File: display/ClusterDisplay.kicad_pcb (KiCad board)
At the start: 4 copper layers, 174.9 x 101.8 mm, 164 parts, among them J1 Verdin iMX95 Hexa 8GB WB IT, J10 RTC coin cell, J11 Molex KK-254 22-27-2041, rota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, J12 Samtec TSW-103-07-G-S A55 con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, J13 Samtec TSW-105-07-G-S USB_1 O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, J14 JST XH B5B-XH-A balanced line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, J15 JST XH B3B-XH-A electret micr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, J16 MFi coprocessor access I2C_1 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, J17 GCT USB4105-GF-A USB-C 2.0 ho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, J2 Phoenix MKDS 1,5/3-5,08 power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, J3 Molex KK-254 22-27-2031 priva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, J4 TST040HDBC-42 panel, J8 Samtec TSW-108-07-G-S JTAG (b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, J9 Samtec TSW-104-07-G-S buttons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, Q1 PMV55ENEA (AEC-Q101, 60V/20V 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, Q2 PMV55ENEA (AEC-Q101, 60V/20V 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, Q3 PMV55ENEA ignition wake pulld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, U1 LM74930-Q1, U10 TLV767-Q1 (3.3 V audio AVDD), U11 TPS2557-Q1, U12 TPD4E05U06-Q1 line-out ESD, U13 TPD4E05U06-Q1 mic ESD, U14 TPD4E05U06-Q1 USB ESD, U2 LM61460-Q1, U3 TLV767-Q1, U4 TCAN1044V-Q1, U6 TPS65131-Q1, U7 TPS61165-Q1, U8 TPS22918-Q1 (AEC-Q100 G2) dia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, U9 TAC5112-Q1

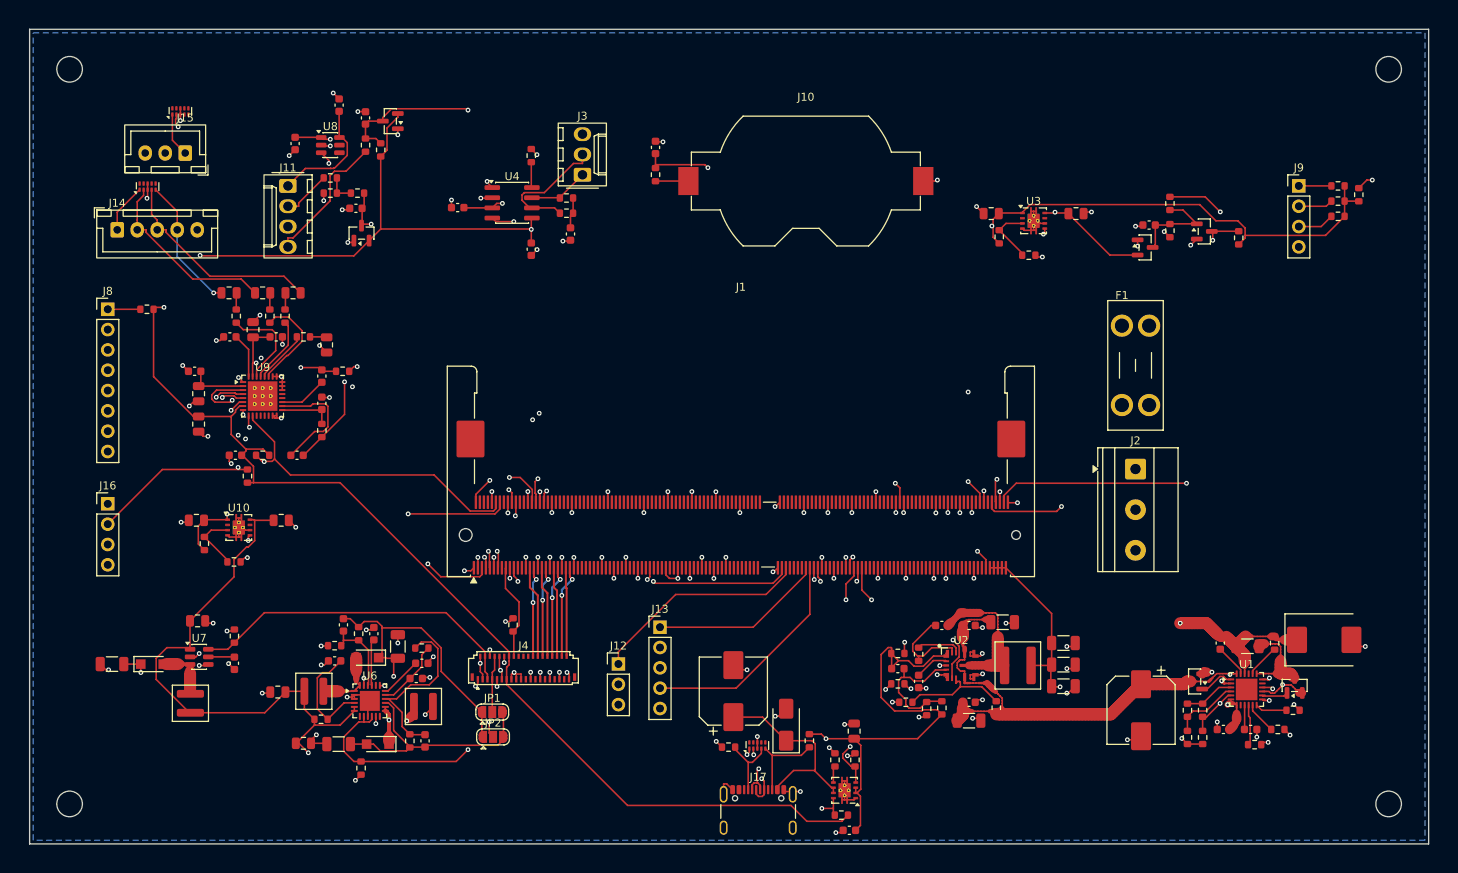
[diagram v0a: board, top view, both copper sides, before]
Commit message: Fix what would stop the boards becoming a product: Verdin mounting, FETs, CarPlay header
Product review 2026-10-18 (docs/electrical-review.md section 8a):
- display: Toradex's four M2 standoffs (S1/S2 2.5 mm module hold-down for
  vibration, S3/S4 7.0 mm for the Verdin Industrial Heatsink) at the design
  guide's Fig 113 positions, GND rings kept on the outer layers; the module
  keepout now follows the real module outline (the module is not centred
  on the socket; the strip under its far edge was open). 178.2 x 105.0 mm.
- display: J16 is a 1x6 MFi daughterboard header with a 5 V supply switched
  by U15 (TPS22918-Q1) from Verdin GPIO_3, as LIVI's carPlayMfiPowerGpio
  expects; the Apple part itself stays on the daughterboard (NDA).
- both: the LM74930 FET pair is Vishay SQJ460AEP (PowerPAK SO-8L, 8.7 mohm,
  IDM 180 A) instead of the NRND SOT-23 PMV55ENEA (X-01, X-02, D-05).
- gauges: 2.2 uH XAL5030-222MEC and 16 V 1210 output caps per the LMR33630
  datasheet (G-14), 1 uF CVS (G-17); inner small gauges at the measured
  +/-118 mm (owner photos), arrows midway between each side's gauges.
- display: 16 V 1210 panel-bias output caps (D-03); bidirectional
  TPD4E02B04-Q1 on the line-out legs (D-11).
- docs: depth stack-up first pass, Toradex supply/thermal/BSP questions,
  an RFQ for wider-temperature small displays, BOM supply-risk note.
Both boards: 0 unconnected, DRC only in the accepted categories, BOM
coverage and fab gate pass; review_netlist gauges 62/62, display only the
pre-existing U6 decoupling distance.

Co-Authored-By: Claude Opus 5.5 <noreply@anthropic.com>
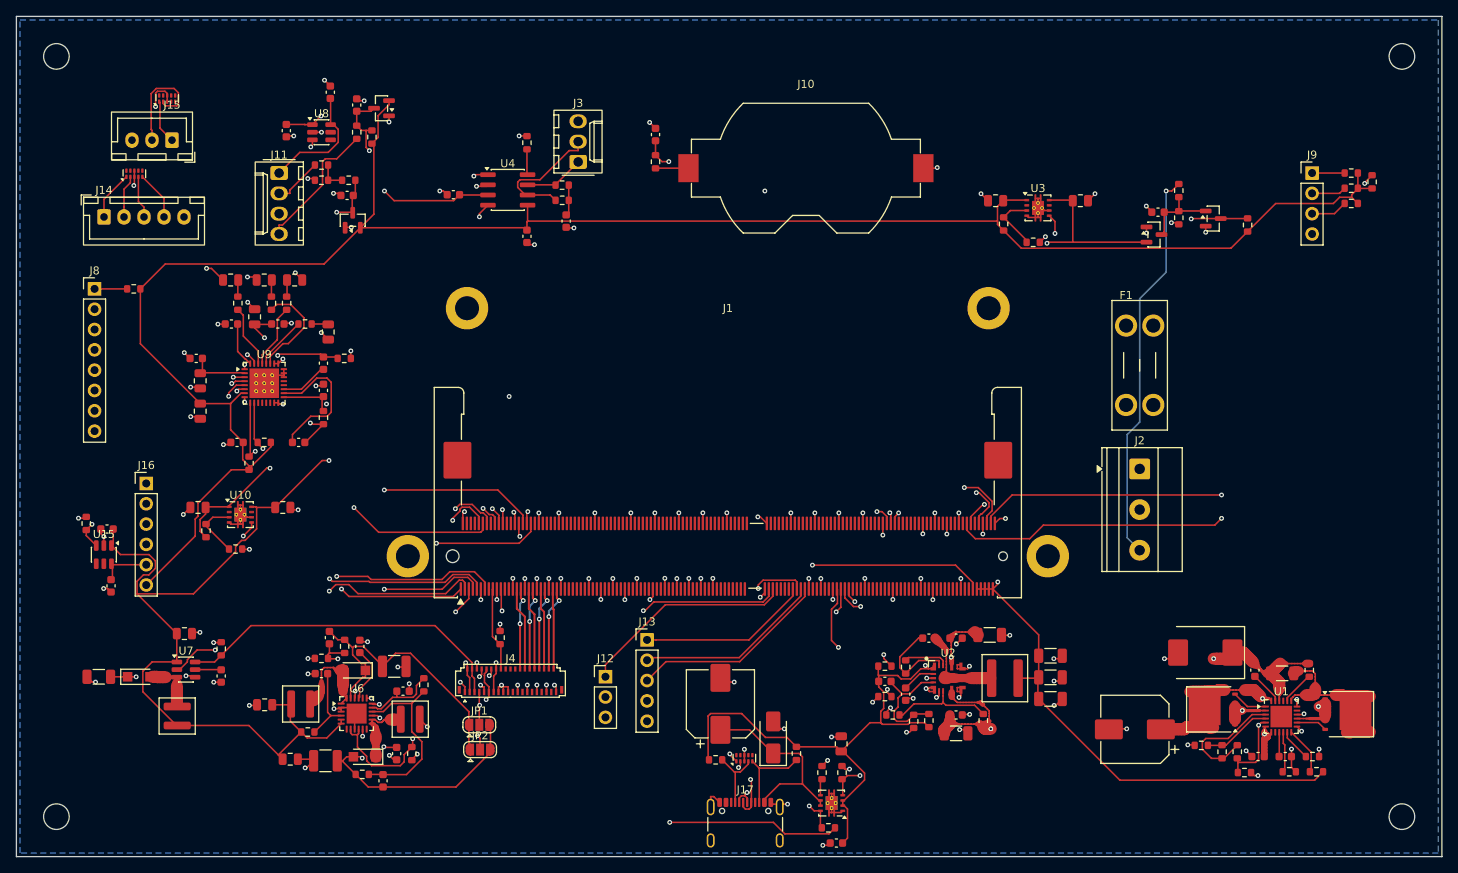
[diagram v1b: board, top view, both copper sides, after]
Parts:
- added C83: 1u MFi switch CIN, Capacitor_SMD:C_0603_1608Metric, F.Cu at (132.2, 160.1)
- added C84: 1u MFi 5V out, Capacitor_SMD:C_0603_1608Metric, F.Cu at (132.7, 167.2)
- added R74: 100k MFi switch off in reset, Resistor_SMD:R_0603_1608Metric, F.Cu at (129.6, 159.4)
- added S1: M2x0.4 SMD standoff 2.5 mm, MountingHole:MountingHole_2.2mm_M2_Pad, F.Cu at (177.2, 132.5)
- added S2: M2x0.4 SMD standoff 2.5 mm, MountingHole:MountingHole_2.2mm_M2_Pad, F.Cu at (242.4, 132.5)
- added S3: M2x0.4 SMD standoff 7.0 mm, MountingHole:MountingHole_2.2mm_M2_Pad, F.Cu at (169.8, 163.5)
- added S4: M2x0.4 SMD standoff 7.0 mm, MountingHole:MountingHole_2.2mm_M2_Pad, F.Cu at (249.8, 163.5)
- added U15: TPS22918-Q1 (AEC-Q100 G2) MFi 5V switch, Package_TO_SOT_SMD:SOT-23-6, F.Cu at (131.8, 163.3)
- C46, C47: footprint Capacitor_SMD:C_1206_3216Metric -> Capacitor_SMD:C_1210_3225Metric
- J16: value MFi coprocessor access I2C_1 + reset (TBD, DNP) -> MFi daughterboard header I2C_1, reset, switched 5V, 1V8 (DNP); footprint Connector_PinHeader_2.54mm:PinHeader_1x04_P2.54mm_Vertical -> Connector_PinHeader_2.54mm:PinHeader_1x06_P2.54mm_Vertical
- Q1: value PMV55ENEA (AEC-Q101, 60V/20V VGS) diode -> SQJ460AEP (AEC-Q101, 60V/20V VGS) diode; footprint Package_TO_SOT_SMD:SOT-23 -> Package_SO:PowerPAK_SO-8L_Single
- Q2: value PMV55ENEA (AEC-Q101, 60V/20V VGS) pass -> SQJ460AEP (AEC-Q101, 60V/20V VGS) pass; footprint Package_TO_SOT_SMD:SOT-23 -> Package_SO:PowerPAK_SO-8L_Single
- U12: value TPD4E05U06-Q1 line-out ESD -> TPD4E02B04-Q1 line-out ESD (bidirectional, review D-11)
- moved D1 15.0 mm to (269.5, 175.5), turned to 180 degrees
- moved C45 11.7 mm to (168.4, 188.1), turned to -90 degrees
- moved R15 8.23 mm to (283.4, 190.4)
- moved Q2 7.45 mm to (287.2, 183.2), turned to 0 degrees
- moved R40 7.28 mm to (164.1, 190.7), turned to 0 degrees
- moved C49 7.24 mm to (166.7, 191.5)
- moved R6 6.83 mm to (274.4, 190.5), turned to 0 degrees
- moved R5 6.76 mm to (273.5, 187.9)
- moved R7 6.76 mm to (271.6, 187.9), turned to 90 degrees
- moved R43 6.60 mm to (170.3, 188.1)
- moved C3 5.50 mm to (275.7, 177.7)
- moved R3 5.50 mm to (282.9, 188.5)
- moved R4 5.50 mm to (280.0, 190.4)
- moved C2 5.50 mm to (276.1, 188.5)
- moved C4 5.50 mm to (279.5, 188.5)
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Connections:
- J1 pad 210: (no net) -> MFI_PWR_EN
- Q1 pad 1: DGATE -> COMMON
- Q1 pad 3: +12V_PROT -> COMMON
- Q2 pad 1: HGATE -> COMMON
- Q2 pad 3: SENSE_OUT -> COMMON
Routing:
- net MFI_PWR_EN: track 0.00 -> 107.3 mm, vias 0 -> 2
- net +1V8: track 318.5 -> 353.5 mm, vias 4 -> 2
- net JTAG_TMS: track 99.1 -> 66.4 mm
- net +12V_PROT: track 65.7 -> 97.9 mm, vias 2 -> 4
- net I2C1_SCL: track 78.9 -> 58.7 mm, vias 3 -> 2
- net RECOVERY: track 69.7 -> 85.3 mm, vias 2 -> 1
- net DIAL_CLICK: track 93.2 -> 108.7 mm, vias 2 -> 3
- net GND: track 207.6 -> 220.8 mm, vias 145 -> 149
- net SENSE_OUT: track 11.3 -> 23.3 mm
- net PANEL_BIAS_EN: track 49.5 -> 37.8 mm
- net MIC_N: track 44.7 -> 55.4 mm, vias 2 -> 1
- net VBACKUP: track 72.9 -> 83.4 mm
- net MFI_RST_N: track 104.6 -> 95.0 mm
- net SW_SENSE: track 6.28 -> 15.8 mm
- net I2S_FSYNC: track 55.2 -> 46.0 mm, vias 3 -> 2
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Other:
- board size 174.9 x 101.8 mm -> 178.2 x 105 mm

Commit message: Six layers with solid GND planes, a field-solved DSI geometry, and the RGB variant routed
Both boards and display-rgb/ move to JLC06161H-3313 six-layer: F / In1 GND /
In2 / In3 with the +5V or +3V3 pour / In4 GND / B. Every net class except GND
is restricted to F, In2, In3 and B in the router input (FreeRouting 2.2.4
ignores a layer_rule "active off"), and review/layout_checks.py now fails a
board with any track on In1 or In4. All three boards: 0 unconnected under
kicad-cli DRC, accepted categories only, no copper but GND fill on the planes.

- DSI pairs are 0.16 mm, field-solved on the new stack-up at 96.4-103.1 ohm
  differential (review/dsi_impedance.py); board minimum track 0.15 mm.
- gauges/ routes VIN_PROT, VIN_FUSED and +5V at 0.4 mm from the start; every
  power net now passes the 20 K current check, and nothing crosses the buck's
  switch node (P-07).
- Panel bias +5.98 V / -6.05 V, inside the ICNL9707's rating; fab/README.md
  gives a diode-test check of the panel's pin polarity before JP1/JP2.
- display-rgb/ brought up to date with display/ (standoffs, FETs, audio,
  USB-C, MFi header), RGB parts renumbered, routed; still not a fab candidate
  while its panel connector is a placeholder.
- FreeRouting runs end at routing: (postroute off) in the DSN, a job timeout
  as backstop; one in-place attempt, since retries of one DSN are identical.
- The OV/UV divider tops are pulled to the LM74930 SW pin.
- docs/electrical-review.md section 8b records the measured results; the
  display/ battery path on inner copper (D-02 residual) is still open.

Co-Authored-By: Claude Opus 5.5 <noreply@anthropic.com>
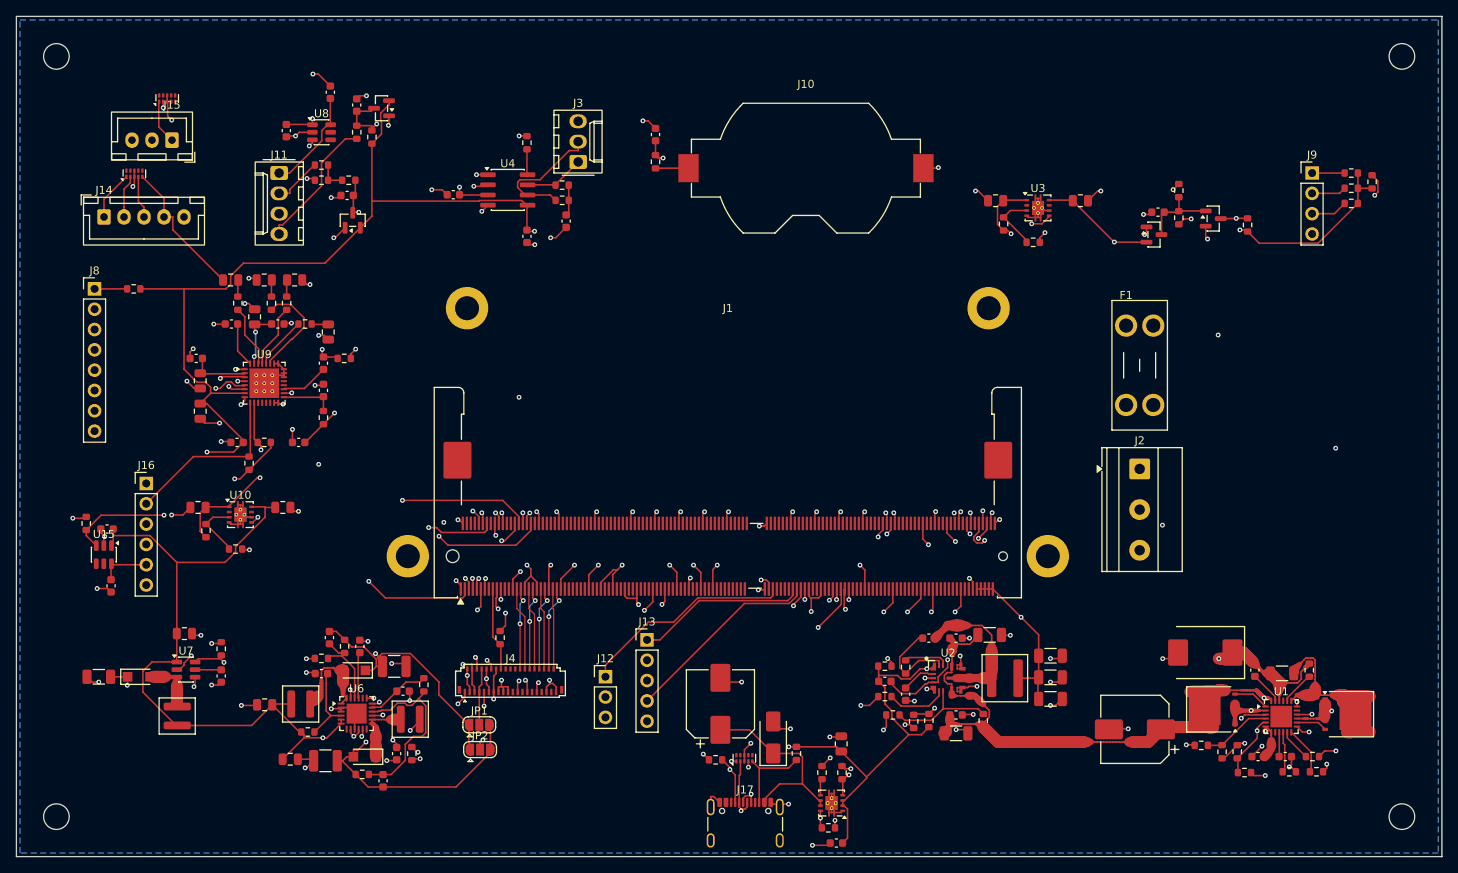
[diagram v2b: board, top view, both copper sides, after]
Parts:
- R38: value 562k VPOS top R1 (see docstring) -> 511k VPOS top R1 (see docstring)
- R40: value 536k VNEG top R3 (see docstring) -> 499k VNEG top R3 (see docstring)
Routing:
- net GND: track 220.8 -> 312.3 mm, vias 149 -> 142
- net +12V_PROT: track 97.9 -> 77.5 mm, vias 4 -> 2
- net DIAL_CLICK: track 108.7 -> 92.4 mm, vias 3 -> 2
- net IGN_WAKE_N: track 57.7 -> 72.5 mm, vias 2 -> 3
- net +1V8: track 353.5 -> 364.4 mm, vias 2 -> 7
- net VBACKUP: track 83.4 -> 72.8 mm
- net MIC_IN_P: track 17.6 -> 7.23 mm, vias 0 -> 2
- net RESET_MICO: track 184.4 -> 194.4 mm
- net I2S_DIN: track 45.7 -> 55.4 mm, vias 2 -> 3
- net MIC_N: track 55.4 -> 46.0 mm, vias 1 -> 2
- net +5V: track 470.7 -> 461.8 mm, vias 6 -> 9
- net I2S_DOUT: track 49.8 -> 58.3 mm
- net I2C1_SCL: track 58.7 -> 67.1 mm, vias 2 -> 1
- net JTAG_TDO: track 67.1 -> 60.2 mm
- net PWR_BTN: track 69.6 -> 76.2 mm
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- added copper zone on In3.Cu, net +5V
- added copper zone on In2.Cu, net GND
- added copper zone on In4.Cu, net GND
- removed copper zone on In2.Cu, net +5V
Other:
- copper layers 4 -> 6

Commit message: Keep the display battery path on outer copper, pour it, and rate it along the real current path
VBAT_IN, VBAT_F, SENSE_OUT, COMMON and +12V_PROT (2.6 A behind the 5 A
fuse) now have their own router net class on F.Cu/B.Cu only, at 0.3 mm
with a 1.0/0.5 mm via, and an F.Cu pour in a 2 mm band around their own
tracks after widening. No battery copper is left on the 0.5 oz inner
layers (about 60 mm of VBAT_F was), on display/ and display-rgb/.

layout_checks.py rates these nets along the path the current takes,
including same-net fill and via barrels, and lists milliamp branches
apart. VBAT_IN and VBAT_F pass on both boards; the remaining necks
(+12V_PROT, COMMON, SENSE_OUT, at most 20 mW each at 2.6 A) are
documented in docs/electrical-review.md section 8b.

route_board.py also gets a hard FreeRouting timeout: a router whose
thread has died never exits. A two-pass route (main path wide, branches
second) was tried and dropped, since FreeRouting 2.2.4 cannot continue
from a board that already has wiring.

Co-Authored-By: Claude Opus 5.5 <noreply@anthropic.com>
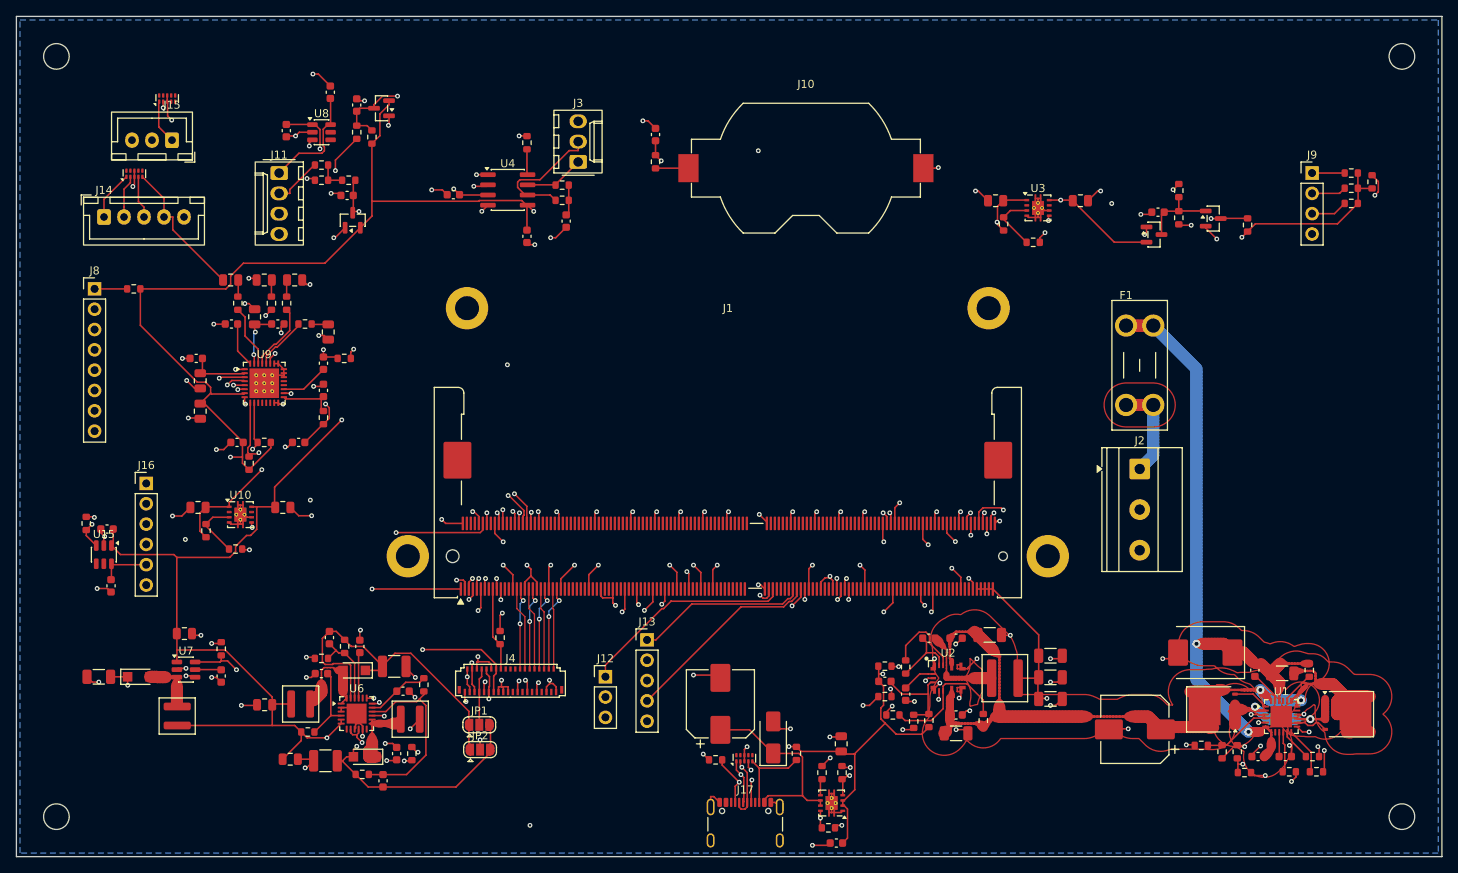
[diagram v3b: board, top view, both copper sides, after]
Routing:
- net IGN_WAKE_N: track 72.5 -> 56.6 mm, vias 3 -> 2
- net +5V: track 461.8 -> 447.3 mm, vias 9 -> 11
- net PWR_BTN: track 76.2 -> 88.7 mm
- net I2S_DIN: track 55.4 -> 45.2 mm, vias 3 -> 2
- net I2C1_SCL: track 67.1 -> 58.1 mm, vias 1 -> 2
- net FB_5V: track 20.3 -> 11.8 mm, vias 2 -> 0
- net +1V8: track 364.4 -> 371.6 mm
- net I2S_BCLK: track 53.3 -> 60.4 mm, vias 2 -> 3
- net I2S_DOUT: track 58.3 -> 51.2 mm, vias 2 -> 3
- net SW_5V: track 18.1 -> 11.3 mm
- net SLEEP_MOCI: track 125.1 -> 119.3 mm
- net AOUT_L_N: track 12.6 -> 7.77 mm, vias 0 -> 2
- net PANEL_VSP: track 37.6 -> 42.2 mm, vias 2 -> 0
- net BOOT_R: track 5.58 -> 10.1 mm
- net IGN_SENSE: track 49.1 -> 53.4 mm
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- added copper zone on F.Cu, net +12V_PROT
- added copper zone on F.Cu, net COMMON
- added copper zone on F.Cu, net SENSE_OUT
- added copper zone on F.Cu, net VBAT_F
- added copper zone on F.Cu, net VBAT_IN
